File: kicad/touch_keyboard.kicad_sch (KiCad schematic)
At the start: 23 parts, among them J1 Conn_02x20_Odd_Even, J2 OUT, J3 Barrel_Jack_Switch, J4 Conn_01x04_Pin, Q1 BC846, Q2 BC846, SW1 SW_Push, U1 Pico

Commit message: circuit update
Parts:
- added H3, H4: MountingHole_Pad, MountingHole:MountingHole_3.2mm_M3_DIN965_Pad, symbol Mechanical:MountingHole_Pad
- added J5: power, Connector_PinHeader_2.54mm:PinHeader_1x02_P2.54mm_Horizontal, symbol Connector:Conn_01x02_Pin
- added R39: 100k, Resistor_SMD:R_0603_1608Metric, symbol Device:R
- added SW2: BT2, 0_local:Button, symbol Switch:SW_Push
- C18, C19: value 1uF -> 10uF
- D1: value MBR0530 -> SK24A; footprint Diode_SMD:D_SOD-123 -> Diode_SMD:D_SMA-SMB_Universal_Handsoldering
- D2, D3: value MBR0530 -> BAT43; footprint Diode_SMD:D_SOD-123 -> Diode_SMD:D_MiniMELF
- J4: footprint Connector_PinHeader_2.54mm:PinHeader_1x04_P2.54mm_Horizontal -> Connector_PinHeader_2.54mm:PinHeader_1x03_P2.54mm_Horizontal; symbol Connector:Conn_01x04_Pin -> Connector:Conn_01x03_Pin
- RV1: footprint Potentiometer_THT:Potentiometer_Bourns_PTV09A-1_Single_Vertical -> 0_local:Potentiometer_Bourns_PTV09A-1_Single_Vertical
- SW1: value SW_Push -> Calibrate; footprint Button_Switch_THT:SW_PUSH-12mm -> 0_local:Button
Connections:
- net +5V: now also J4.3 (Pin_3); no longer J4.2 (Pin_2)
- net GND: now also RV1.3, H3.1, H4.1, J5.1 (Pin_1), SW2.1; no longer J4.4 (Pin_4), RV1.1
- net TX: now also U1.1 (GPIO0); no longer U1.6 (GPIO4)
- net led_out: now also U1.32 (GPIO27_ADC1); no longer U1.31 (GPIO26_ADC0)
- net mode: now also U1.31 (GPIO26_ADC0); no longer U1.29 (GPIO22)
- net VREF: now reaches U1.35 (ADC_VREF)
- net VREF: now also RV1.1, R39.1; no longer RV1.3
- net at D3.1 (K), Q2.3 (C), R37.1: now also J4.2 (Pin_2); no longer J4.3 (Pin_3)
- net at C18.2, D1.2 (A), J3.1: now also J5.2 (Pin_2)
- net at J1.1 (Pin_1), R38.1: now also R39.2
- net bt_in renamed bt2
- net bt2: now also SW2.2; no longer SW1.2
- new net cal_bt: SW1.2, U1.6 (GPIO4)
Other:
- moved on the sheet: RV1

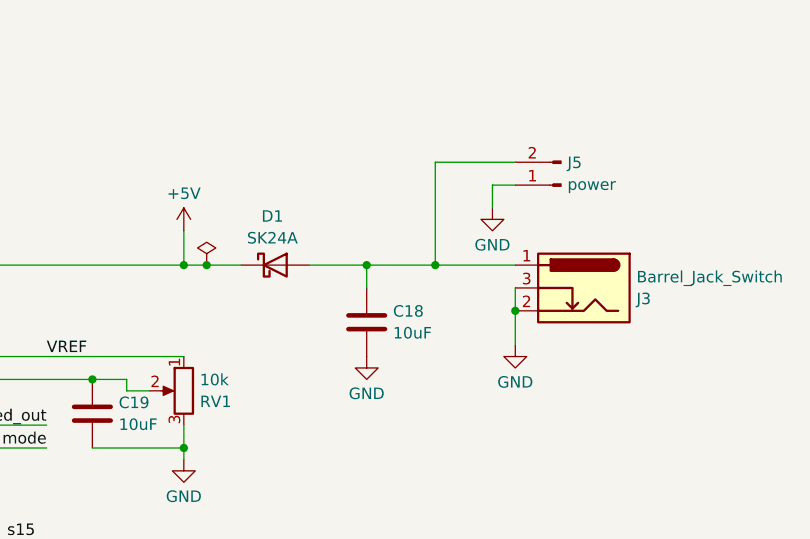
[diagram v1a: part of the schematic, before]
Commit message: update to the current version of the hardware
includes pcb2gcode config and post-processing script
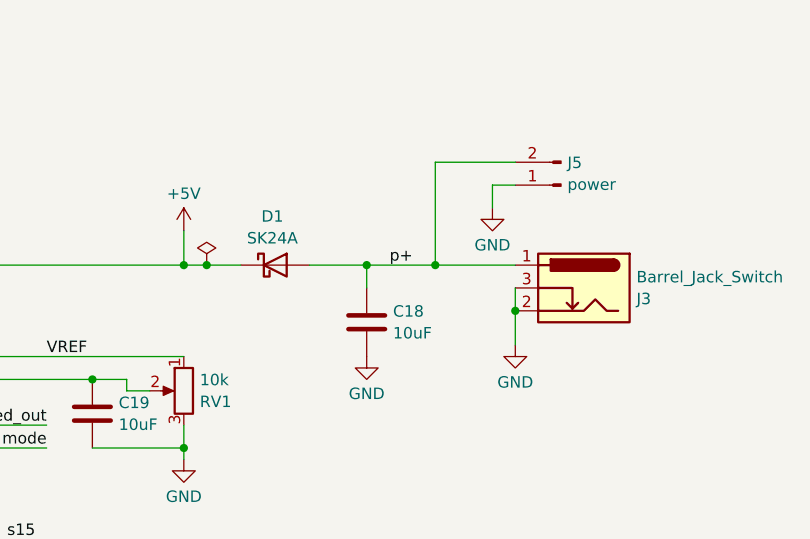
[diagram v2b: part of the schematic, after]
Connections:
- net p+: now reaches C18.2, D1.2 (A), J3.1, J5.2 (Pin_2)
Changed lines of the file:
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@@
     (effects (font (size 1.27 1.27)) (justify right bottom))
+  )
+  (label "p+" (at 233.68 46.99 0) (fields_autoplaced)
+    (effects (font (size 1.27 1.27)) (justify left bottom))
   )
   (label "s02" (at 82.55 49.53 180) (fields_autoplaced)
@@
     )
   )
-  (symbol (lib_id "Diode:MBR0530") (at 215.9 118.11 180) (unit 1)
+  (symbol (lib_name "MBR0530_1") (lib_id "Diode:MBR0530") (at 215.9 118.11 180) (unit 1)
     (in_bom yes) (on_board yes) (dnp no) (fields_autoplaced)
     (property "Reference" "D2" (at 216.2175 112.6957 0)
